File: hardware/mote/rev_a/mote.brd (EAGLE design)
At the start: 160 x 100 mm, 110 parts, among them J1 TC2030-JLINK-L, Q1 CSD22206W, Q10 CSD22206W, Q11 CSD22206W, Q2 CSD75207W15, Q3 CSD75207W15, Q4 CSD13303W1015, Q5 CSD22206W, Q6 CSD22206W, Q7 CSD22206W, Q8 CSD22206W, Q9 CSD22206W, U1 NRF52840, U10 MS5637-02BA03, U3 MAX17222, U4 AMN41121, U5 SI7021-A20-GM1, U6 ISL29125, U7 MAX44009, U8 LIS2DW12, U9 AB1815-T3, X1 7V-32.000MAHV-T, X3 ABS07-32.768KHZ-7-T

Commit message: use mppt front end
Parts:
- removed D2, D3: DIODE_SCHOTTKYMBR0520LT1G, passives:SOD123
- removed Q1, Q5: CSD22206W, fets:DSBGA
- removed Q2, Q3: CSD75207W15, fets:DSBGA
- removed Q4: CSD13303W1015, fets:6DSBGA
- removed TP2, TP3, TP4, TP5, TP6, TP7, TP8, TP9: TEST_POINT_0.040IN, headers:TESTPOINT_0.040IN
- removed U2: (no value), chips:WLCSP-6
- added C26, C27, C28: (no value), passives:0603_CAP
- added L2: (no value), passives:IHL-2525CZ
- added R15, R16, R17, R18, R19, R20, R21, R22: (no value), passives:0402_RES
- added U11: ADP5091, chips:QFN-24-4MM
- R1: value 1kΩ -> (none)
- R3: value 20Ω -> (none)
- R5, R6: value 100kΩ -> (none)
- moved R1 475.3 mm to (-114.3, -494.0)
- moved R3 471.6 mm to (-114.3, -497.8)
- moved R5 445.9 mm to (-114.3, -501.6)
- moved R6 413.4 mm to (-114.3, -505.5)
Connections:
- removed net SRC_SW: D3.A, Q4.A2, Q5.A1, R6.1, TP3.TESTPOINT
- new net N$30: C26.1, U11.8
- new net N$32: R21.2, R22.1, U11.9
- new net N$38: C28.1, D1.+, L2.P$2, R22.2, TP1.TESTPOINT, U11.10
- new net N$45: L2.P$1, U11.13
- new net N$47: C27.1, U11.14, U11.15
- net GND: now also C26.2, C27.2, C28.2, R16.1, R17.1, R18.1, R19.1, R20.1, R21.1, U11.12, U11.7, U11.GND_PAD; no longer Q4.B2, Q4.C2, R3.1, U2.A2, U2.B2
- net N$1: now also R1.1, R16.2, U11.2; no longer D2.A, Q4.A1, Q4.B1, Q4.C1, Q5.C1, Q5.C2, Q5.C3, R5.1, TP4.TESTPOINT
- net N$10: now also R1.2, R3.2, R5.2, R6.2, U11.1; no longer Q2.B1, TP7.TESTPOINT
- net N$11: now also R15.2, R3.1, U11.5; no longer Q1.A1, R1.1, TP2.TESTPOINT, U2.C2
- net N$13: now also R15.1, R17.2, U11.6; no longer D2.K, Q2.A1, Q2.C1, R5.2, TP5.TESTPOINT
- net N$16: now also R18.2, R5.1, U11.3; no longer Q3.B1, TP8.TESTPOINT
- net N$17: now also R19.2, R6.1, U11.4; no longer Q1.A2, Q1.A3, Q1.B1, Q1.B2, Q1.B3, R3.2
- net N$18: now also R20.2, U11.21; no longer D3.K, Q3.A1, Q3.C1, R6.2, TP6.TESTPOINT
- net VBAT: now also U11.18; no longer Q3.A2, Q3.A3, Q3.B3, TP9.TESTPOINT
- net VSW: now also U11.16, U11.17; no longer D1.+, Q1.C1, Q1.C2, Q1.C3, Q2.A2, Q2.A3, Q2.B2, Q2.B3, Q2.C2, Q2.C3, Q3.B2, Q3.C2, Q3.C3, Q5.A2, Q5.A3, Q5.B1, Q5.B2, Q5.B3, R1.2, TP1.TESTPOINT, U2.A1, U2.C1

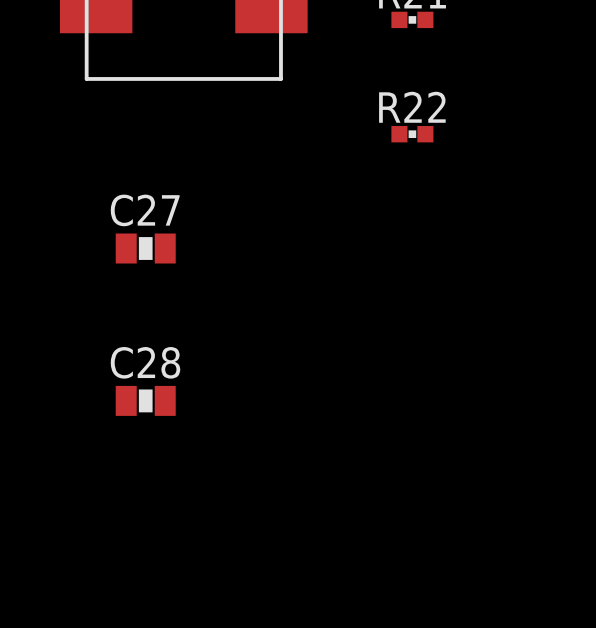
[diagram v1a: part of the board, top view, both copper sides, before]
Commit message: add component values for mppt
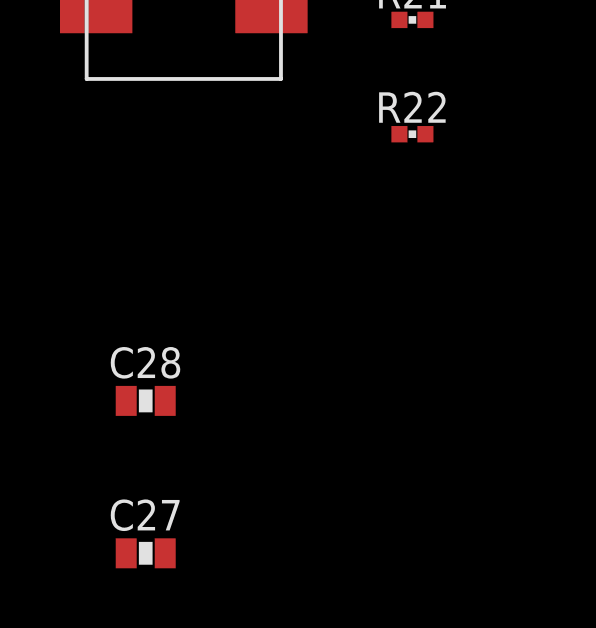
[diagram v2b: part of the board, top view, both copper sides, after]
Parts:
- C26: value (none) -> 10nF
- C27, C28: value (none) -> 10uF
- R1, R16: value (none) -> 5MΩ
- R15: value (none) -> 115kΩ
- R17: value (none) -> 3.48MΩ
- R18: value (none) -> 4.53MΩ
- R19: value (none) -> 5.76MΩ
- R20: value (none) -> 150kΩ
- R21: value (none) -> 18MΩ
- R22: value (none) -> 4.7MΩ
- R3: value (none) -> 6.6MΩ
- R5: value (none) -> 5.49MΩ
- R6: value (none) -> 4.22MΩ
- moved C27 10.2 mm to (-123.2, -553.7)
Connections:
- net GND: now also U11.23, U11.24
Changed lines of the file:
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@@
 <attribute name="MPN" value="ADP5091ACPZ-1-R7" x="-111.76" y="-487.68" size="1.778" layer="27" display="off"/>
 </element>
-<element name="R1" library="passives" package="0402_RES" value="" x="-114.3" y="-494.03"/>
-<element name="R3" library="passives" package="0402_RES" value="" x="-114.3" y="-497.84"/>
-<element name="R5" library="passives" package="0402_RES" value="" x="-114.3" y="-501.65"/>
-<element name="R6" library="passives" package="0402_RES" value="" x="-114.3" y="-505.46"/>
-<element name="R15" library="passives" package="0402_RES" value="" x="-114.3" y="-509.27"/>
-<element name="R16" library="passives" package="0402_RES" value="" x="-114.3" y="-513.08"/>
-<element name="R17" library="passives" package="0402_RES" value="" x="-114.3" y="-516.89"/>
-<element name="R18" library="passives" package="0402_RES" value="" x="-114.3" y="-520.7"/>
-<element name="R19" library="passives" package="0402_RES" value="" x="-114.3" y="-524.51"/>
-<element name="R20" library="passives" package="0402_RES" value="" x="-114.3" y="-528.32"/>
-<element name="C26" library="passives" package="0603_CAP" value="" x="-114.3" y="-532.13">
+<element name="R1" library="passives" package="0402_RES" value="5MΩ" x="-114.3" y="-494.03"/>
+<element name="R3" library="passives" package="0402_RES" value="6.6MΩ" x="-114.3" y="-497.84"/>
+<element name="R5" library="passives" package="0402_RES" value="5.49MΩ" x="-114.3" y="-501.65"/>
+<element name="R6" library="passives" package="0402_RES" value="4.22MΩ" x="-114.3" y="-505.46"/>
+<element name="R15" library="passives" package="0402_RES" value="115kΩ" x="-114.3" y="-509.27"/>
+<element name="R16" library="passives" package="0402_RES" value="5MΩ" x="-114.3" y="-513.08"/>
+<element name="R17" library="passives" package="0402_RES" value="3.48MΩ" x="-114.3" y="-516.89"/>
+<element name="R18" library="passives" package="0402_RES" value="4.53MΩ" x="-114.3" y="-520.7"/>
+<element name="R19" library="passives" package="0402_RES" value="5.76MΩ" x="-114.3" y="-524.51"/>
+<element name="R20" library="passives" package="0402_RES" value="150kΩ" x="-114.3" y="-528.32"/>
+<element name="C26" library="passives" package="0603_CAP" value="10nF" x="-114.3" y="-532.13">
 <attribute name="DIGIKEY" value="490-3896-2-ND" x="-114.3" y="-532.13" size="1.778" layer="27" display="off"/>
 </element>
-<element name="R21" library="passives" package="0402_RES" value="" x="-114.3" y="-535.94"/>
-<element name="R22" library="passives" package="0402_RES" value="" x="-114.3" y="-539.75"/>
+<element name="R21" library="passives" package="0402_RES" value="18MΩ" x="-114.3" y="-535.94"/>
+<element name="R22" library="passives" package="0402_RES" value="4.7MΩ" x="-114.3" y="-539.75"/>
 <element name="L2" library="passives" package="IHL-2525CZ" value="" x="-121.92" y="-534.67">
 <attribute name="DIGIKEY" value="541-2562-1-ND" x="-121.92" y="-534.67" size="1.778" layer="27" display="off"/>
 </element>
-<element name="C27" library="passives" package="0603_CAP" value="" x="-123.19" y="-543.56">
-<attribute name="DIGIKEY" value="490-3896-2-ND" x="-123.19" y="-543.56" size="1.778" layer="27" display="off"/>
+<element name="C28" library="passives" package="0603_CAP" value="10uF" x="-123.19" y="-548.64">
+<attribute name="DIGIKEY" value="490-3896-2-ND" x="-123.19" y="-548.64" size="1.778" layer="27" display="off"/>
 </element>
-<element name="C28" library="passives" package="0603_CAP" value="" x="-123.19" y="-548.64">
-<attribute name="DIGIKEY" value="490-3896-2-ND" x="-123.19" y="-548.64" size="1.778" layer="27" display="off"/>
+<element name="C27" library="passives" package="0603_CAP" value="10uF" x="-123.19" y="-553.72">
+<attribute name="DIGIKEY" value="490-3896-2-ND" x="-123.19" y="-553.72" size="1.778" layer="27" display="off"/>
 </element>
 </elements>
@@
 <contactref element="C26" pad="2"/>
 <contactref element="R21" pad="1"/>
-<contactref element="C27" pad="2"/>
 <contactref element="C28" pad="2"/>
 <contactref element="TP27" pad="TESTPOINT"/>
@@
 <contactref element="U11" pad="GND_PAD"/>
 <contactref element="U11" pad="7"/>
+<contactref element="U11" pad="23"/>
+<contactref element="U11" pad="24"/>
+<contactref element="C27" pad="2"/>
 <wire x1="-82.73" y1="-156.21" x2="-82.11693125" y2="-163.83" width="0" layer="19" extent="1-1"/>
 <wire x1="-74.49693125" y1="-160.02" x2="-82.11693125" y2="-163.83" width="0" layer="19" extent="1-1"/>
@@
 <wire x1="-95.25" y1="-440.69" x2="-95.25" y2="-425.45" width="0" layer="19" extent="1-1"/>
 <wire x1="-108.694" y1="-442.486" x2="-95.25" y2="-440.69" width="0" layer="19" extent="1-1"/>
-<wire x1="-111.76" y1="-487.68" x2="-108.694" y2="-442.486" width="0" layer="19" extent="1-1"/>
+<wire x1="-112.51" y1="-485.68" x2="-108.694" y2="-442.486" width="0" layer="19" extent="1-1"/>
+<wire x1="-113.01" y1="-485.68" x2="-112.51" y2="-485.68" width="0" layer="19" extent="1-1"/>
+<wire x1="-111.76" y1="-487.68" x2="-112.51" y2="-485.68" width="0" layer="19" extent="1-1"/>
 <wire x1="-113.01" y1="-489.68" x2="-111.76" y2="-487.68" width="0" layer="19" extent="1-1"/>
 <wire x1="-110.51" y1="-489.68" x2="-111.76" y2="-487.68" width="0" layer="19" extent="1-1"/>
@@
 <wire x1="-113.65" y1="-532.13" x2="-114.73306875" y2="-528.32" width="0" layer="19" extent="1-1"/>
 <wire x1="-114.73306875" y1="-535.94" x2="-113.65" y2="-532.13" width="0" layer="19" extent="1-1"/>
-<wire x1="-122.54" y1="-543.56" x2="-114.73306875" y2="-535.94" width="0" layer="19" extent="1-1"/>
-<wire x1="-122.54" y1="-548.64" x2="-122.54" y2="-543.56" width="0" layer="19" extent="1-1"/>
+<wire x1="-122.54" y1="-548.64" x2="-114.73306875" y2="-535.94" width="0" layer="19" extent="1-1"/>
+<wire x1="-122.54" y1="-553.72" x2="-122.54" y2="-548.64" width="0" layer="19" extent="1-1"/>
 </signal>
 <signal name="N$8">
@@
 <contactref element="U11" pad="14"/>
 <contactref element="C27" pad="1"/>
-<wire x1="-109.76" y1="-488.43" x2="-123.84" y2="-543.56" width="0" layer="19" extent="1-1"/>
+<wire x1="-109.76" y1="-488.43" x2="-123.84" y2="-553.72" width="0" layer="19" extent="1-1"/>
 <wire x1="-109.76" y1="-487.93" x2="-109.76" y2="-488.43" width="0" layer="19" extent="1-1"/>
 </signal>

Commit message: small visual changes
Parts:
- L2: value (none) -> 22uH
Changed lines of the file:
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@@
 <element name="R21" library="passives" package="0402_RES" value="18MΩ" x="-114.3" y="-535.94"/>
 <element name="R22" library="passives" package="0402_RES" value="4.7MΩ" x="-114.3" y="-539.75"/>
-<element name="L2" library="passives" package="IHL-2525CZ" value="" x="-121.92" y="-534.67">
+<element name="L2" library="passives" package="IHL-2525CZ" value="22uH" x="-121.92" y="-534.67">
 <attribute name="DIGIKEY" value="541-2562-1-ND" x="-121.92" y="-534.67" size="1.778" layer="27" display="off"/>
 </element>

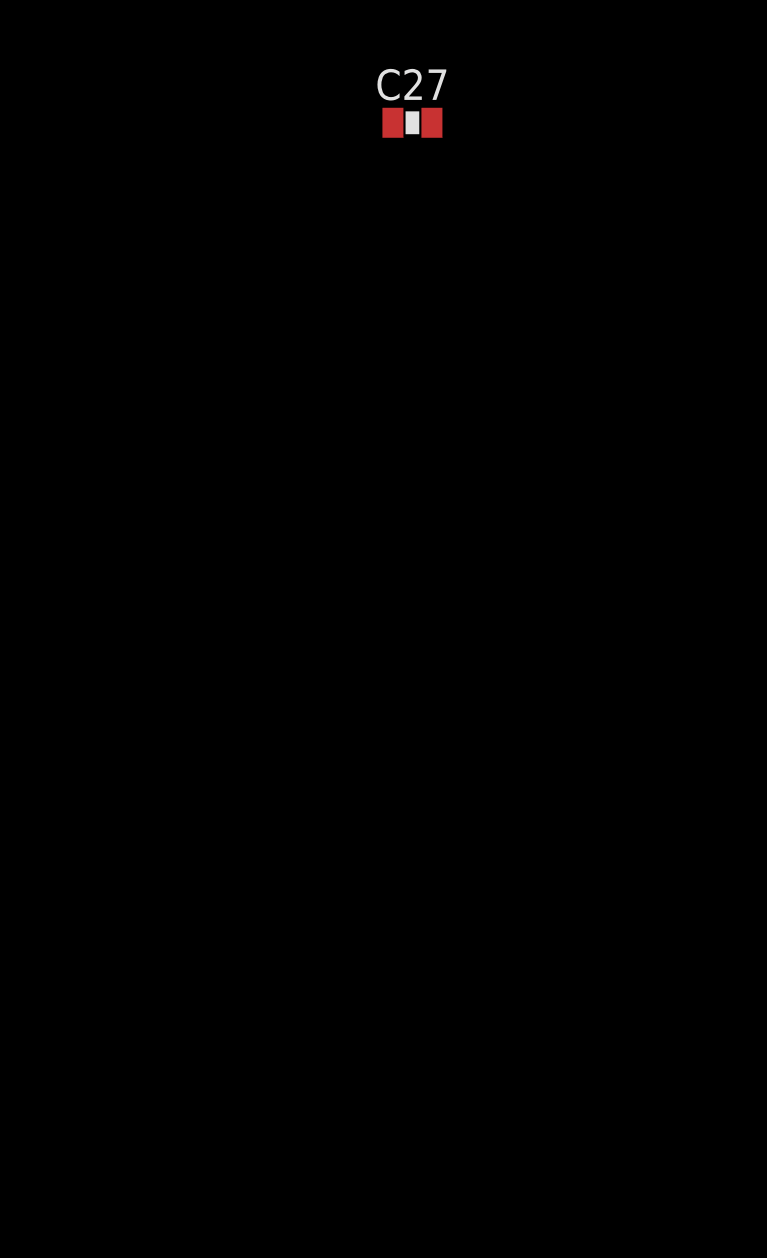
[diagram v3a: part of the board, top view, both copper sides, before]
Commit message: Fix some issues from design review
See #1

adc to vsw
reverse power gate fets
decoup caps before fet
pullups on interrupts
gate i2c
enable dc-dc mode for dcc
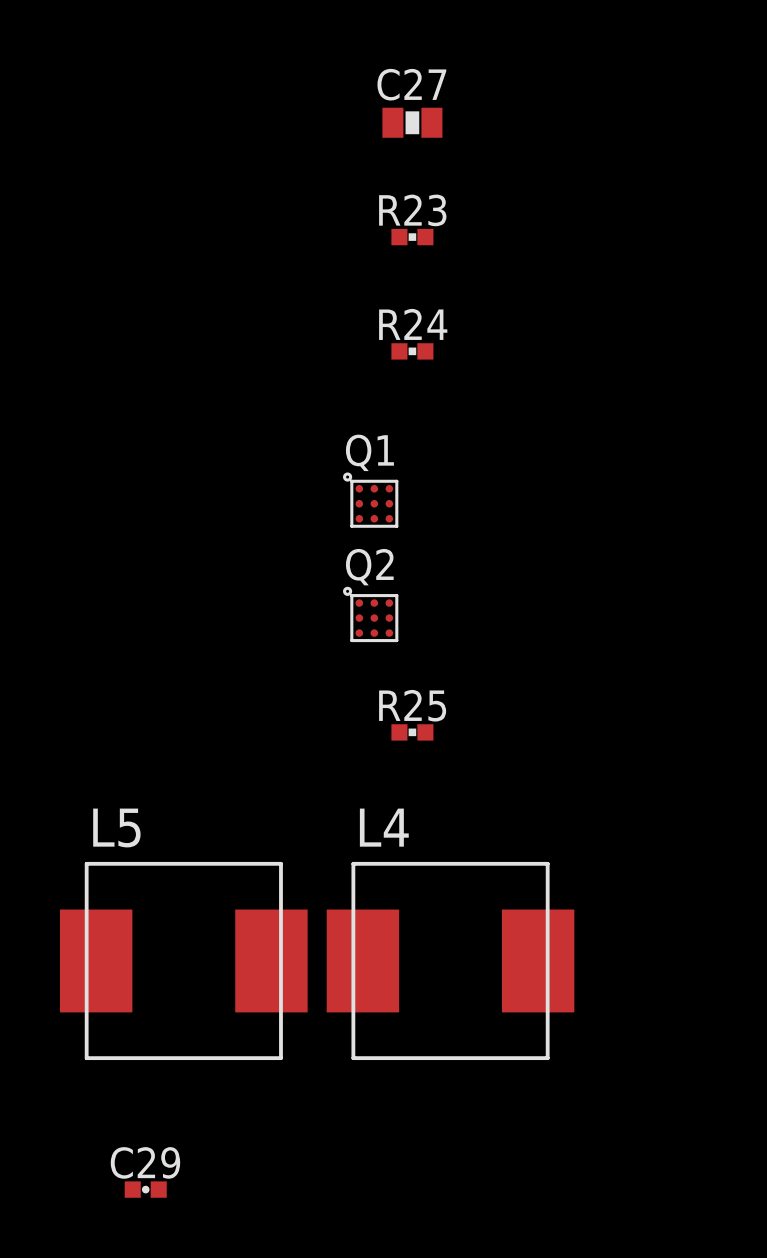
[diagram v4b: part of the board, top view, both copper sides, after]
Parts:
- added C29: 47nF, passives:0402_CAP
- added L4: 10uH, passives:IHL-2525CZ
- added L5: 15nH, passives:IHL-2525CZ
- added Q1, Q2: CSD22206W, fets:DSBGA
- added R23, R24: 10kΩ, passives:0402_RES
- added R25: 100MΩ, passives:0402_RES
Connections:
- removed net N$35: JP4.1, Q9.C1, Q9.C2, Q9.C3, R12.2, TP18.TESTPOINT
- new net !I2C_EN: Q1.A1, Q2.A1, R25.1, U1.R1
- new net N$31: Q7.C1, Q7.C2, Q7.C3, U6.1
- new net N$40: C17.1, C9.1, JP1.1, Q6.A2, Q6.A3, Q6.B1, Q6.B2, Q6.B3, R9.2, TP12.TESTPOINT
- new net N$41: Q1.C1, Q1.C2, Q1.C3, R8.2
- new net N$44: L4.P$2, U1.B3
- new net N$46: L4.P$1, L5.P$2
- net !CLR_INT: now also R23.1
- net !LT_INT: now also R24.1
- net GND: now also C29.2
- net N$15: now also Q6.C1, Q6.C2, Q6.C3; no longer C17.1, C9.1, Q6.A2, Q6.A3, Q6.B1, Q6.B2, Q6.B3
- net N$19: now also C18.1, JP4.1, Q9.A2, Q9.A3, Q9.B1, Q9.B2, Q9.B3, R12.2, TP18.TESTPOINT; no longer C10.1, C20.1, Q7.A2, Q7.A3, Q7.B1, Q7.B2, Q7.B3, U6.1
- net N$20: now also Q8.C1, Q8.C2, Q8.C3; no longer C21.1, Q8.A2, Q8.A3, Q8.B1, Q8.B2, Q8.B3
- net N$21: now also Q9.C1, Q9.C2, Q9.C3; no longer C18.1, Q9.A2, Q9.A3, Q9.B1, Q9.B2, Q9.B3
- net N$22: now also Q10.C1, Q10.C2, Q10.C3; no longer C19.1, Q10.A2, Q10.A3, Q10.B1, Q10.B2, Q10.B3
- net N$23: now also Q11.C1, Q11.C2, Q11.C3; no longer Q11.A2, Q11.A3, Q11.B1, Q11.B2, Q11.B3
- net N$24: now also Q11.A2, Q11.A3, Q11.B1, Q11.B2, Q11.B3; no longer Q11.C1, Q11.C2, Q11.C3
- net N$3: now also C29.1, L5.P$1, U1.E24
- net N$33: now also C10.1, C20.1, Q7.A2, Q7.A3, Q7.B1, Q7.B2, Q7.B3, R23.2; no longer Q7.C1, Q7.C2, Q7.C3
- net N$34: now also Q2.C1, Q2.C2, Q2.C3, R7.2; no longer JP3.1, Q8.C1, Q8.C2, Q8.C3, R11.2, TP16.TESTPOINT
- net N$36: now also C19.1, Q10.A2, Q10.A3, Q10.B1, Q10.B2, Q10.B3; no longer Q10.C1, Q10.C2, Q10.C3
- net N$37: now also C21.1, JP3.1, Q8.A2, Q8.A3, Q8.B1, Q8.B2, Q8.B3, R11.2, R24.2, TP16.TESTPOINT; no longer JP1.1, Q6.C1, Q6.C2, Q6.C3, R9.2, TP12.TESTPOINT
- net PIR_OUT: no longer U1.R1
- net SW: now also U1.J1
- net VCC: now also Q1.A2, Q1.A3, Q1.B1, Q1.B2, Q1.B3, Q2.A2, Q2.A3, Q2.B1, Q2.B2, Q2.B3, R25.2; no longer R7.2, R8.2

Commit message: add NRF51822
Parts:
- removed L4: 10uH, passives:IHL-2525CZ
- removed L5: 15nH, passives:IHL-2525CZ
- added A3: FRACTUS-2.4GHZ-FR05-S1-N-0-102, chips:FRACTUS-ANTENNA-FR05-S1-N-0-102
- added B2: BAL-NRF01D3, chips:BAL-NRF01D3
- added C30, C31, C46, C47, C52, C53: 12pF, passives:0402_CAP
- added C42: 0.1uF, passives:0402_CAP
- added C43, C48: 1nF, passives:0402_CAP
- added C44: 4.7uF, passives:0402_CAP
- added C45: 1uF, passives:0402_CAP
- added C49: 47nF, passives:0402_CAP
- added C50: 2.2nF, passives:0402_CAP
- added C51: 0.8pF, passives:0402_CAP
- added J2: TC2030-JLINK-NL, connector:TC2030-IDC-NL
- added L6, L8: 15nH, passives:0402_CAP
- added L7, L9: 10uH, passives:0603_CAP
- added R29: 12k, passives:0402_RES
- added U12: NRF51822QF, chips:QFN-48-6MM
- added X2, X6: ABS05-32.768KHZ-9-T, crystals:ABS05
- added X5: 16MHz, crystals:TXC-8Y
- A1: value (none) -> FRACTUS-2.4GHZ-FR05-S1-N-0-102; device chips:AH212M -> chips:FRACTUS-ANTENNA-FR05-S1-N-0-102
- moved C29 669.1 mm to (48.0, 55.1)
- moved A1 31.9 mm to (32.3, 50.5)
- moved C14 0.63 mm to (44.5, 53.5)
- moved C5 0.63 mm to (44.5, 52.7)
- moved C11 0.25 mm to (54.4, 52.9)
- moved C15 0.25 mm to (48.0, 54.1)
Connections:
- removed net N$46: L4.P$1, L5.P$2
- new net AVDD1: C43.1, C45.1, L8.1, U12.35, U12.36
- new net DCC1: L9.2, U12.2
- new net N$49: L6.2, L7.1
- new net N$60: B2.ANT1, U12.31
- new net N$61: B2.ANT2, U12.32
- new net N$62: A3.1, B2.SE, C51.1
- new net N$63: L8.2, L9.1
- new net N$64: C46.1, U12.37, X5.1
- new net N$65: C47.1, U12.38, X5.3
- new net N$66: C48.1, U12.39
- new net N$67: C49.1, U12.29
- new net NRF_A2: C53.1, U12.46, X6.B
- new net NRF_A3: C52.1, U12.45, X6.A
- new net NRF_SWDCLK: J2.4, R29.1, U12.24
- new net NRF_SWDIO/!RESET: J2.2, J2.6, U12.23
- new net NRF_VCC: C42.1, C44.1, J2.1, U12.1, U12.12
- new net VDD_PA1: B2.VCC, C50.1, U12.30
- new net VSEC: BAT1.+, U1.A12, U11.17
- new net XL1: C31.2, U1.D2, X2.A
- new net XL2: C30.2, U1.F2, X2.B
- net !CLR_EN: now also U1.AD16; no longer U1.B15
- net !CLR_INT: now also U1.W24; no longer U1.T23
- net !HUM_EN: now also U1.U1; no longer U1.B19
- net !I2C_EN: no longer U1.R1
- net !PR_EN: now also U1.R1; no longer U1.B17
- net !RST: now also J1.3, U1.AD12
- net ACC_CS: now also U1.AD10; no longer U1.AD12
- net ACC_INT2: now also U1.L24; no longer U1.P23
- net CLKOUT: no longer U1.D2
- net GND: now also B2.GND, C30.1, C31.1, C42.2, C43.2, C44.2, C45.2, C46.2, C47.2, C48.2, C49.2, C50.2, C51.2, C52.2, C53.2, J2.5, R29.2, U12.13, U12.33, U12.34, U12.GND; no longer U1.F2
- net MISO: now also U1.AD22; no longer U1.AD10
- net MOSI: now also U1.AD20; no longer U1.AC9
- net N$3: now also L6.1; no longer L5.P$1
- net N$44: now also L7.2; no longer L4.P$2
- net N$6: now also A1.1; no longer A1.P1
- net PIR_OUT: now also U1.Y23; no longer U1.V23
- net RTC_CS: now also U1.AD8; no longer U1.AC11
- net SCK: now also U1.AD18; no longer U1.AD8
- net SCL: now also U1.N1; no longer U1.H2
- net SDA: now also U1.L1; no longer U1.G1
- net SW: now also U1.G1; no longer U1.AD20
- net VBAT: now also U1.A10; no longer U1.B13
- net VSW: no longer BAT1.+, U1.A12, U11.17
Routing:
- net NRF_VCC: track 0.00 -> 21.7 mm, vias 0 -> 3
- net AVDD1: track 0.00 -> 17.7 mm, vias 0 -> 2
- net GND: track 11.1 -> 19.5 mm, vias 3 -> 24
- net NRF_A3: track 0.00 -> 5.15 mm
- net NRF_A2: track 0.00 -> 4.97 mm
- net N$64: track 0.00 -> 4.88 mm
- net XL1: track 0.00 -> 4.64 mm
- net NRF_SWDIO/!RESET: track 0.00 -> 4.60 mm
- net N$65: track 0.00 -> 4.32 mm
- net NRF_SWDCLK: track 0.00 -> 4.32 mm
- net N$62: track 0.00 -> 3.30 mm
- net N$3: track 1.66 -> 4.90 mm
- net XL2: track 0.00 -> 3.24 mm
- net DCC1: track 0.00 -> 2.58 mm
- net VDD_PA1: track 0.00 -> 2.46 mm
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- added copper zone on layer 1, net N$35
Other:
- board text added: "RESET"
